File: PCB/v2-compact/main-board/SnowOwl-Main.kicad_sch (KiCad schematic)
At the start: 0 parts

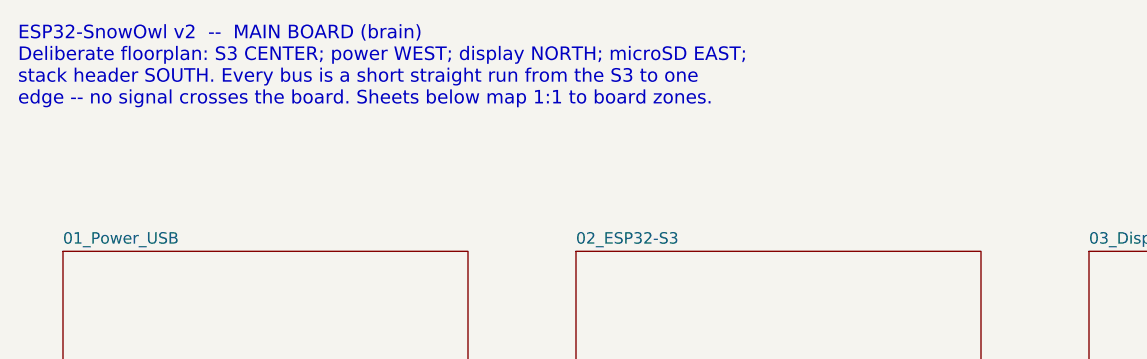
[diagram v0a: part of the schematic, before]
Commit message: PCB: rework main board to phone-style layout; J1 -> horizontal strip
Main board (per feedback) is now a phone-style split — front is pure UI, back
carries the electronics:
- FRONT: status LEDs at the very top (above the display), TFT rotated to
  LANDSCAPE (sideways), nav buttons below it and moved down. Same feel as the
  ESP32-DIV, sideways screen.
- BACK: ESP32-S3 behind the display, microSD beside it, power + USB-C at the
  bottom-centre edge like a phone.

To keep the centre column free for the landscape display and the bottom-centre
USB-C, J1 is reoriented from a vertical 2x10 to a HORIZONTAL 10x2 strip in the
lower-centre. J1 is the shared mating datum, so the shield's J1 moves to match;
the shield's RV1106 / HTRC110 / bulk-cap zones shift to sit above/below the new
strip (SPI spine still runs north from it). Every v1 capability unchanged.

Updated both .kicad_pcb, both floorplan SVGs, both schematics' zone specs, and
PLACEMENT.md. Verified: files parse, J1 clears all zones, no same-side overlaps.

Co-Authored-By: Claude <noreply@anthropic.com>
Claude-Session: https://claude.ai/code/session_017BEAKBRVwbUCc7Sa2o3Ye7
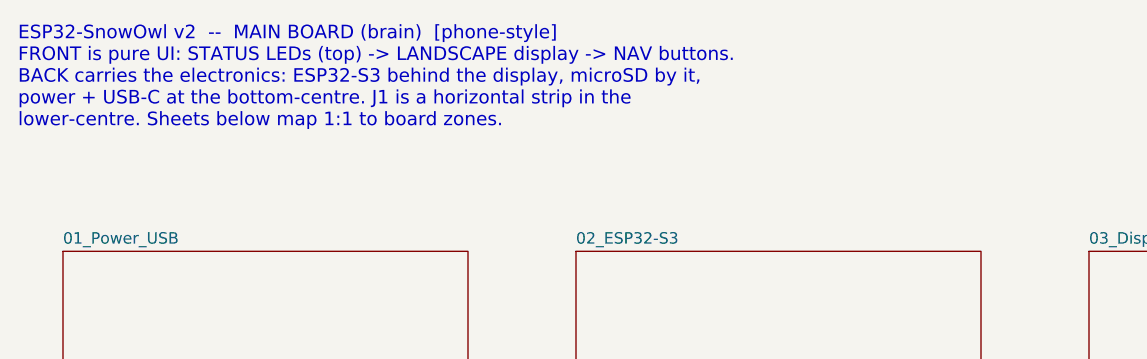
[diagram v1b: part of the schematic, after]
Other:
- note added: "ESP32-SnowOwl v2 -- MAIN BOARD (brain) [phone-style] FRONT is pure UI: STATUS LEDs (top) -> LANDSCAPE display -> NAV buttons. BACK carries the electronics: ESP32-S3 behind the display, microSD by it, power + USB-C at the bottom-centre. J1 is a horizontal strip in the lower-centre. Sheets below map 1:1 to board zones."
- note removed: "ESP32-SnowOwl v2 -- MAIN BOARD (brain) Deliberate floorplan: S3 CENTER; power WEST; display NORTH; microSD EAST; stack header SOUTH. Every bus is a short straight run from the S3 to one edge -- no signal crosses the board. Sheets below map 1:1 to board zones."
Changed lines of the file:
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@@
   (title_block (title "SnowOwl v2 - Main Board") (company "YurilLAB")
     (comment 1 "ESP32-SnowOwl v2 - compact 2-board stack"))
-  (text "ESP32-SnowOwl v2  --  MAIN BOARD (brain)
-Deliberate floorplan: S3 CENTER; power WEST; display NORTH; microSD EAST;
-stack header SOUTH. Every bus is a short straight run from the S3 to one
-edge -- no signal crosses the board. Sheets below map 1:1 to board zones." (at 20 15 0)
+  (text "ESP32-SnowOwl v2  --  MAIN BOARD (brain)  [phone-style]
+FRONT is pure UI: STATUS LEDs (top) -> LANDSCAPE display -> NAV buttons.
+BACK carries the electronics: ESP32-S3 behind the display, microSD by it,
+power + USB-C at the bottom-centre. J1 is a horizontal strip in the
+lower-centre. Sheets below map 1:1 to board zones." (at 20 15 0)
     (effects (font (size 1.5 1.5)) (justify left top)))
   (sheet (at 25.0 40.0) (size 45.0 24.0) (fields_autoplaced)
@@
   (sheet_instances
     (path "/" (page "1"))
-    (path "/5a16f03e-7720-4196-8935-02486c7f4d92" (page "2"))
-    (path "/69eeae04-e414-457c-9281-e752e6b089ca" (page "3"))
-    (path "/1dec575f-7e00-41f4-9a42-99bca7336f8e" (page "4"))
-    (path "/b1c1ada6-64db-4671-be35-d468ae6c24ca" (page "5"))
-    (path "/ea40565a-6ea5-45e8-bb37-926bc3bcd3cd" (page "6"))
+    (path "/5781769a-7303-419b-8493-73073849aff7" (page "2"))
+    (path "/db14e0c1-d42f-42fe-a29f-93976d88e738" (page "3"))
+    (path "/5f352b60-5f6a-4255-98c6-3cd3a1e5b1fb" (page "4"))
+    (path "/c59edb49-d9d8-4ec8-ad65-2bc40d2804a7" (page "5"))
+    (path "/6b0fca45-c8ee-4426-946f-24f4ba9a3d95" (page "6"))
   )
 )
